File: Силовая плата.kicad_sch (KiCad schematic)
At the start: 9 parts, among them Q1 2N6660, Q2 2N6660, Q3 2N6660, Q4 2N6660, Q5 2N6660, Q6 2N6660, U1 HIP2100_SOIC, U2 HIP2100_SOIC, U3 HIP2100_SOIC

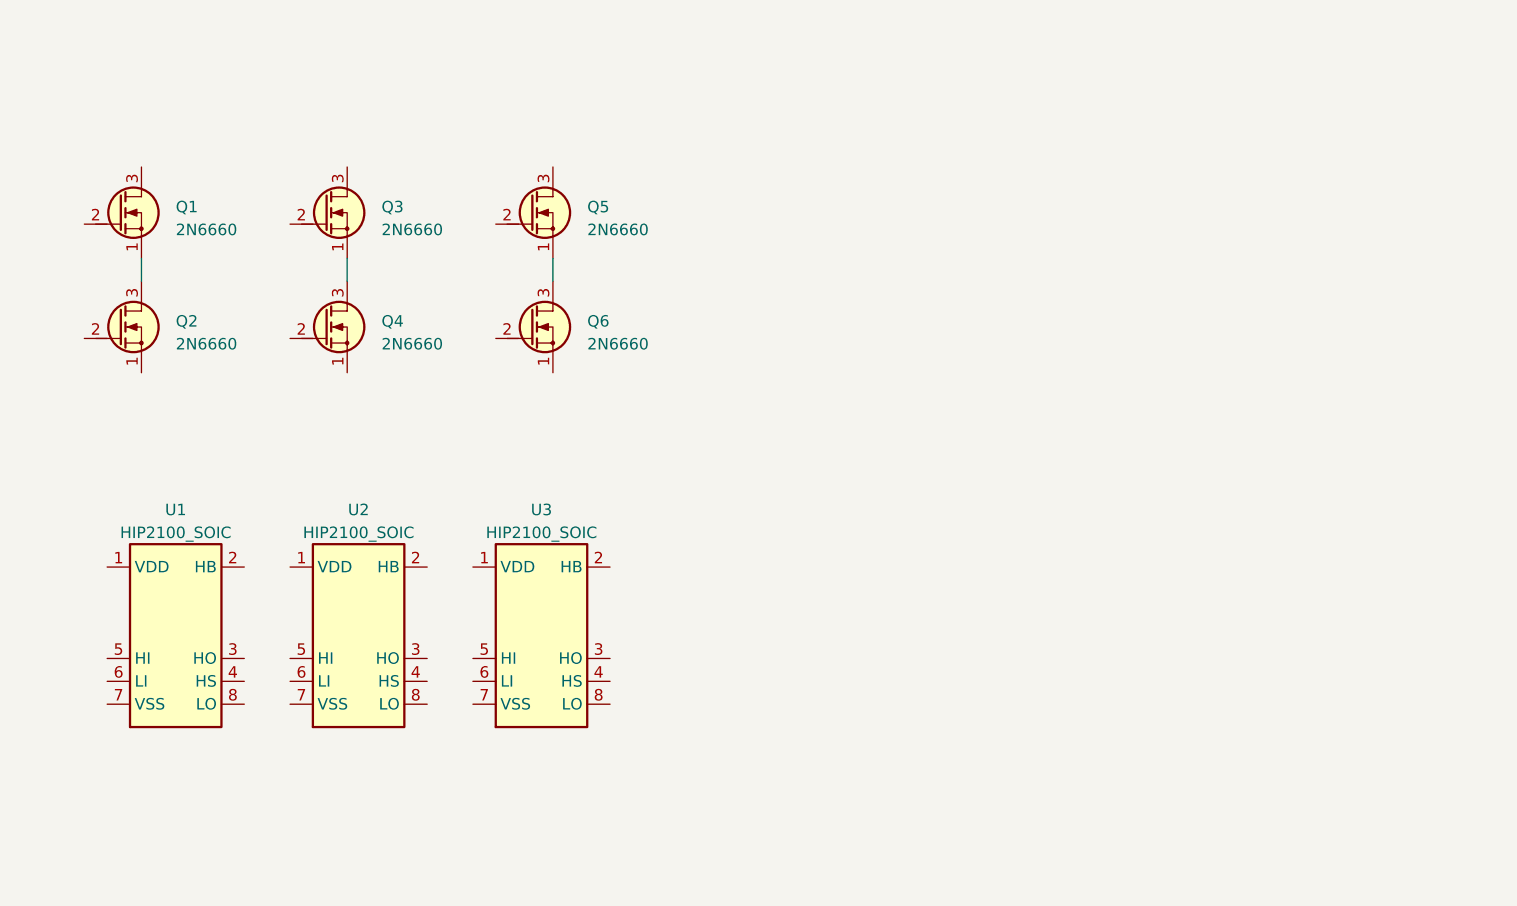
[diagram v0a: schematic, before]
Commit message: Добавил датчики тока и шунты
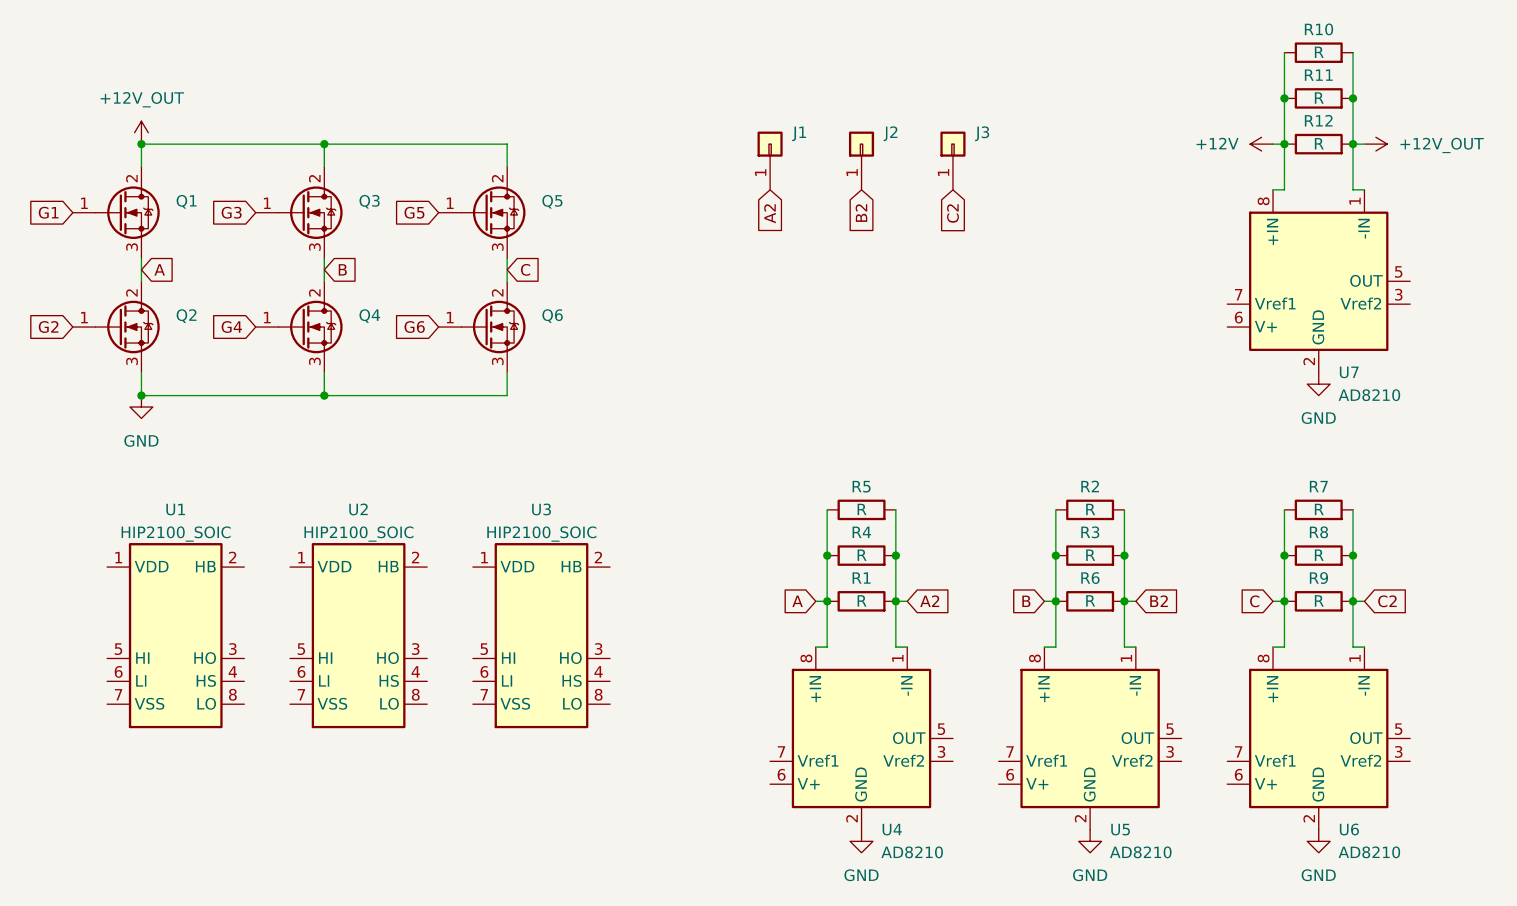
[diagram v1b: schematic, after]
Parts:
- removed Q1, Q2, Q3, Q4, Q5, Q6: 2N6660, Package_SON:Infineon_PG-TDSON-8_6.15x5.15mm, symbol PCM_Transistor_MOSFET_AKL:2N6660
- added J1, J2, J3: Conn_01x01, symbol Connector_Generic:Conn_01x01
- added Q1, Q2, Q3, Q4, Q5, Q6: BSP89, Package_TO_SOT_SMD:TO-263-2, symbol Transistor_FET:BSP89
- added R1, R10, R11, R12, R2, R3, R4, R5, R6, R7, R8, R9: R, Resistor_SMD:R_2512_6332Metric_Pad1.40x3.35mm_HandSolder, symbol Device:R
- added U4, U5, U6, U7: AD8210, Package_SO:SOIC-8_3.9x4.9mm_P1.27mm, symbol Amplifier_Current:AD8210
- U1, U2, U3: footprint Package_DFN_QFN:DFN-8-1EP_3x3mm_P0.5mm_EP1.65x2.38mm -> Package_SO:SOIC-8_3.9x4.9mm_P1.27mm
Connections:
- new net +12V: Q1.2 (D), Q3.2 (D), Q5.2 (D), R10.1, R10.2, R11.1, R11.2, R12.1, R12.2, U7.1 (-IN), U7.8 (+IN)
- new net A: Q1.3 (S), Q2.2 (D), R1.1, R4.1, R5.1, U4.8 (+IN)
- new net A2: J1.1 (Pin_1), R1.2, R4.2, R5.2, U4.1 (-IN)
- new net B: Q3.3 (S), Q4.2 (D), R2.1, R3.1, R6.1, U5.8 (+IN)
- new net B2: J2.1 (Pin_1), R2.2, R3.2, R6.2, U5.1 (-IN)
- new net C: Q5.3 (S), Q6.2 (D), R7.1, R8.1, R9.1, U6.8 (+IN)
- new net C2: J3.1 (Pin_1), R7.2, R8.2, R9.2, U6.1 (-IN)
- new net G1: Q1.1 (G)
- new net G2: Q2.1 (G)
- new net G3: Q3.1 (G)
- new net G4: Q4.1 (G)
- new net G5: Q5.1 (G)
- new net G6: Q6.1 (G)
- new net GND: Q2.3 (S), Q4.3 (S), Q6.3 (S), U4.2 (GND), U5.2 (GND), U6.2 (GND), U7.2 (GND)

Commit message: Начальная версия
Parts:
- removed J1, J2, J3: Conn_01x01, symbol Connector_Generic:Conn_01x01
- removed Q1, Q2, Q3, Q4, Q5, Q6: BSP89, Package_TO_SOT_SMD:TO-263-2, symbol Transistor_FET:BSP89
- removed R1, R10, R11, R12, R2, R3, R4, R5, R6, R7, R8, R9: R, Resistor_SMD:R_2512_6332Metric_Pad1.40x3.35mm_HandSolder, symbol Device:R
- removed U1, U2, U3: HIP2100_SOIC, Package_SO:SOIC-8_3.9x4.9mm_P1.27mm, symbol Driver_FET:HIP2100_SOIC
- removed U4, U5, U6, U7: AD8210, Package_SO:SOIC-8_3.9x4.9mm_P1.27mm, symbol Amplifier_Current:AD8210
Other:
- added sheet Connector (Connector.kicad_sch)
- added sheet Driver (Driver.kicad_sch)
- added sheet Measure (Measure.kicad_sch)
- added sheet Power (Power.kicad_sch)
- added sheet Temperture (Temperture.kicad_sch)

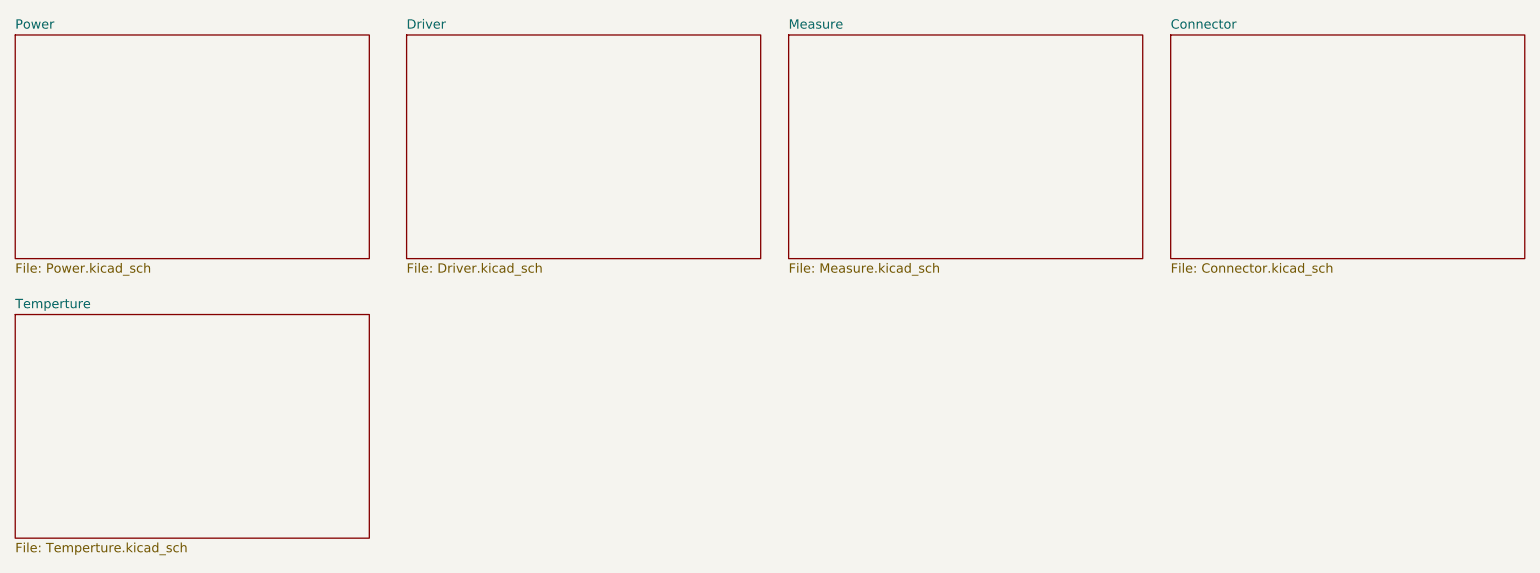
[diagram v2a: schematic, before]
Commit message: Перенес защиту от переполюсовки и добавил керамику
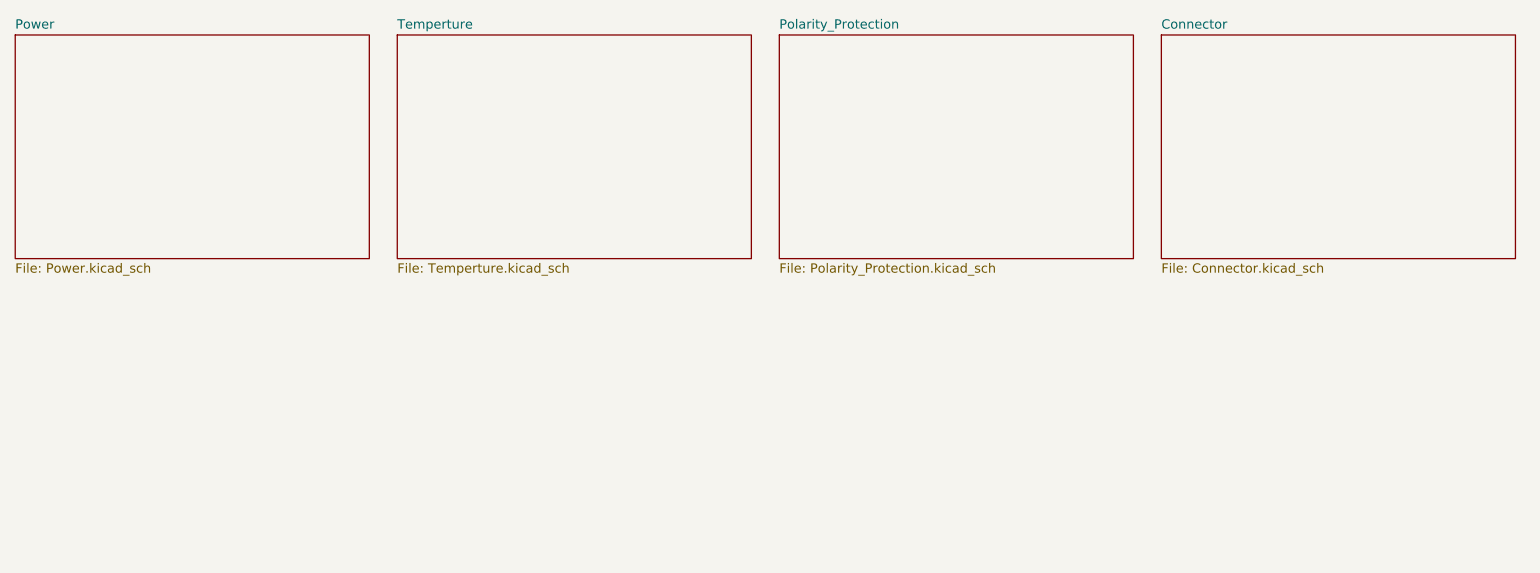
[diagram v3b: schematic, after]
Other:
- sheet Measure renamed Polarity_Protection
- removed sheet Driver
- sheet Polarity_Protection: file Measure.kicad_sch -> Polarity_Protection.kicad_sch
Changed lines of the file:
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@@
 (kicad_sch (version 20230121) (generator eeschema)
   (paper "A4")
-  (sheet (at 25.4 57.15) (size 48.26 30.48) (fields_autoplaced)
+  (sheet (at 77.47 19.05) (size 48.26 30.48) (fields_autoplaced)
     (stroke (width 0.1524) (type solid))
     (fill (color 0 0 0 0.0000))
-    (property "Sheetname" "Temperture" (at 25.4 56.4384 0)
+    (property "Sheetname" "Temperture" (at 77.47 18.3384 0)
       (effects (font (size 1.27 1.27)) (justify left bottom))
     )
-    (property "Sheetfile" "Temperture.kicad_sch" (at 25.4 88.2146 0)
+    (property "Sheetfile" "Temperture.kicad_sch" (at 77.47 50.1146 0)
       (effects (font (size 1.27 1.27)) (justify left top))
     )
-    (property "Поле2" "" (at 25.4 57.15 0)
+    (property "Поле2" "" (at 77.47 19.05 0)
       (effects (font (size 1.27 1.27)) hide)
     )
@@
     )
   )
-  (sheet (at 130.81 19.05) (size 48.26 30.48) (fields_autoplaced)
+  (sheet (at 129.54 19.05) (size 48.26 30.48) (fields_autoplaced)
     (stroke (width 0.1524) (type solid))
     (fill (color 0 0 0 0.0000))
-    (property "Sheetname" "Measure" (at 130.81 18.3384 0)
+    (property "Sheetname" "Polarity_Protection" (at 129.54 18.3384 0)
       (effects (font (size 1.27 1.27)) (justify left bottom))
     )
-    (property "Sheetfile" "Measure.kicad_sch" (at 130.81 50.1146 0)
+    (property "Sheetfile" "Polarity_Protection.kicad_sch" (at 129.54 50.1146 0)
       (effects (font (size 1.27 1.27)) (justify left top))
     )
-    (property "Поле2" "" (at 130.81 19.05 0)
+    (property "Поле2" "" (at 129.54 19.05 0)
+      (effects (font (size 1.27 1.27)) hide)
+    )
+    (property "Поле3" "" (at 129.54 19.05 0)
       (effects (font (size 1.27 1.27)) hide)
     )
@@
     )
   )
-  (sheet (at 78.74 19.05) (size 48.26 30.48) (fields_autoplaced)
+  (sheet (at 181.61 19.05) (size 48.26 30.48) (fields_autoplaced)
     (stroke (width 0.1524) (type solid))
     (fill (color 0 0 0 0.0000))
-    (property "Sheetname" "Driver" (at 78.74 18.3384 0)
+    (property "Sheetname" "Connector" (at 181.61 18.3384 0)
       (effects (font (size 1.27 1.27)) (justify left bottom))
     )
-    (property "Sheetfile" "Driver.kicad_sch" (at 78.74 50.1146 0)
+    (property "Sheetfile" "Connector.kicad_sch" (at 181.61 50.1146 0)
       (effects (font (size 1.27 1.27)) (justify left top))
     )
-    (property "Поле2" "" (at 78.74 19.05 0)
+    (property "Поле2" "" (at 181.61 19.05 0)
       (effects (font (size 1.27 1.27)) hide)
     )
-    (instances
-      (project "Силовая плата"
-        (path "/96c6fc92-8ec6-44f7-b0dc-9ad8f1acea09" (page "3"))
-      )
-    )
-  )
-  (sheet (at 182.88 19.05) (size 48.26 30.48) (fields_autoplaced)
-    (stroke (width 0.1524) (type solid))
-    (fill (color 0 0 0 0.0000))
-    (property "Sheetname" "Connector" (at 182.88 18.3384 0)
-      (effects (font (size 1.27 1.27)) (justify left bottom))
-    )
-    (property "Sheetfile" "Connector.kicad_sch" (at 182.88 50.1146 0)
-      (effects (font (size 1.27 1.27)) (justify left top))
-    )
-    (property "Поле2" "" (at 182.88 19.05 0)
-      (effects (font (size 1.27 1.27)) hide)
-    )

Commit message: Добавил документы
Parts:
- added C1, C10, C11, C12, C13, C14, C15, C16, C17, C18, C19, C2, C20, C21, C22, C23, C24, C25, C26, C27, C28, C29, C3, C30, C31, C32, C33, C34, C35, C36, C37, C38, C39, C4, C40, C41, C42, C43, C44, C45, C5, C6, C9: 10u, Capacitor_SMD:C_1210_3225Metric_Pad1.33x2.70mm_HandSolder, symbol Device:C_Small
- added C46, C47, C48: 0.1u, Capacitor_SMD:C_0603_1608Metric_Pad1.08x0.95mm_HandSolder, symbol Device:C_Small
- added C7, C8: 2200p, Capacitor_THT:C_Disc_D7.5mm_W5.0mm_P7.50mm, symbol Device:C
- added D1: BZT52C10, Diode_SMD:D_SOD-123, symbol Device:D_Zener_Small
- added D2, D3, D4: STLM75DS2F, Package_SO:MSOP-8_3x3mm_P0.65mm, symbol Temperature_My:STLM75DS2F
- added H1, H2, H3, H4: MountingHole, MountingHole:MountingHole_3.2mm_M3, symbol Mechanical:MountingHole
- added J1, J5: A, Connector_My:Power_Wire, symbol Connector_Generic:Conn_01x01
- added J1: IN+, Connector_My:Power_Wire, symbol Connector_Generic:Conn_01x01
- added J2: IN-, Connector_My:Power_Wire, symbol Connector_Generic:Conn_01x01
- added J4: Conn_02x10_Odd_Even, Connector_PinSocket_2.54mm:PinSocket_2x10_P2.54mm_Vertical, symbol Connector_Generic:Conn_02x10_Odd_Even
- added J6: B, Connector_My:Power_Wire, symbol Connector_Generic:Conn_01x01
- added J7: C, Connector_My:Power_Wire, symbol Connector_Generic:Conn_01x01
- added Q1: BSS214NW, MOSFET_My:IPTG007N06NM5ATMA1, symbol Transistor_FET:BSS214NW
- added Q2, Q3, Q4, Q5, Q6, Q7: 2N7002, MOSFET_My:IPTG007N06NM5ATMA1, symbol Transistor_FET:2N7002
- added R1: 0.5m, Resistor_SMD:R_2512_6332Metric_Pad1.40x3.35mm_HandSolder, symbol Device:R
- added R1: 100k, Resistor_SMD:R_0805_2012Metric_Pad1.20x1.40mm_HandSolder, symbol Device:R_Small
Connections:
- new net: C7.2, J2.1 (Pin_1), Q1.3 (D)
- new net: D1.1 (K), Q1.1 (G), R1.1
- new net +24V: C1.1, C10.1, C11.1, C12.1, C13.1, C14.1, C15.1, C16.1, C17.1, C18.1, C19.1, C2.1, C20.1, C21.1, C22.1, C23.1, C24.1, C25.1, C26.1, C27.1, C28.1, C29.1, C3.1, C30.1, C31.1, C32.1, C33.1, C34.1, C35.1, C36.1, C37.1, C38.1, C39.1, C4.1, C40.1, C41.1, C42.1, C43.1, C44.1, C45.1, C5.1, C6.1, C8.1, C9.1, J1.1 (Pin_1), J4.17 (Pin_17), J4.19 (Pin_19), R1.1, R1.2
- new net +3.3V: C46.1, C47.1, C48.1, D2.7 (A0), D2.8 (VDD), D3.6 (A1), D3.8 (VDD), D4.6 (A1), D4.7 (A0), D4.8 (VDD), J4.1 (Pin_1)
- new net A: J4.13 (Pin_13), J5.1 (Pin_1), Q2.2 (S), Q3.3 (D)
- new net B: J4.5 (Pin_5), J6.1 (Pin_1), Q4.2 (S), Q5.3 (D)
- new net C: J4.14 (Pin_14), J7.1 (Pin_1), Q6.2 (S), Q7.3 (D)
- new net Earth_Protective: C7.1, C8.2, J1.1 (Pin_1)
- new net G1: J4.11 (Pin_11), Q2.1 (G)
- new net G2: J4.7 (Pin_7), Q3.1 (G)
- new net G3: J4.3 (Pin_3), Q4.1 (G)
- new net G4: J4.8 (Pin_8), Q5.1 (G)
- new net G5: J4.16 (Pin_16), Q6.1 (G)
- new net G6: J4.12 (Pin_12), Q7.1 (G)
- new net GND: C1.2, C10.2, C11.2, C12.2, C13.2, C14.2, C15.2, C16.2, C17.2, C18.2, C19.2, C2.2, C20.2, C21.2, C22.2, C23.2, C24.2, C25.2, C26.2, C27.2, C28.2, C29.2, C3.2, C30.2, C31.2, C32.2, C33.2, C34.2, C35.2, C36.2, C37.2, C38.2, C39.2, C4.2, C40.2, C41.2, C42.2, C43.2, C44.2, C45.2, C46.2, C47.2, C48.2, C5.2, C6.2, C9.2, D1.2 (A), D2.4 (GND), D2.5 (A2), D2.6 (A1), D3.4 (GND), D3.5 (A2), D3.7 (A0), D4.4 (GND), D4.5 (A2), J4.10 (Pin_10), J4.15 (Pin_15), J4.18 (Pin_18), J4.9 (Pin_9), Q1.2 (S), Q3.2 (S), Q5.2 (S), Q7.2 (S)
- new net SCL_MCU: D2.2 (SCL), D3.2 (SCL), D4.2 (SCL), J4.4 (Pin_4)
- new net SDA_MCU: D2.1 (SDA), D3.1 (SDA), D4.1 (SDA), J4.6 (Pin_6)
- new net Shunt_2: J4.20 (Pin_20), Q2.3 (D), Q4.3 (D), Q6.3 (D), R1.2
- new net ~{OS}_MCU: D2.3 (~{OS}/INT), D3.3 (~{OS}/INT), D4.3 (~{OS}/INT), J4.2 (Pin_2)
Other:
- removed sheet Connector
- removed sheet Polarity_Protection
- removed sheet Power
- removed sheet Temperture
- note added: "Адрес: 1001001"
- note added: "Адрес: 1001010"
- note added: "Адрес: 1001011"
- note added: "Защита от переполюсовки"
- note added: "Крепежные отверстия"
- note added: "Разъём на плату ууправления"
- note added: "Силовая часть"
- note added: "Температура фазы А"
- note added: "Температура фазы В"
- note added: "Температура фазы С"
- note added: "Фильтрующие конденсаторы"
- title: (none) -> Плата силовая ЭЛТ схема электрическая принципиальная
